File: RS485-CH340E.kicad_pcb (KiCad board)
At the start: 2 copper layers, 16.9 x 14.4 mm, 17 parts, among them J1 USB_A, J2 Conn_01x04_Male, SW1 SW_SPDT, U1 CH340E, U2 SP3485CN, U3 XC6206P332MR

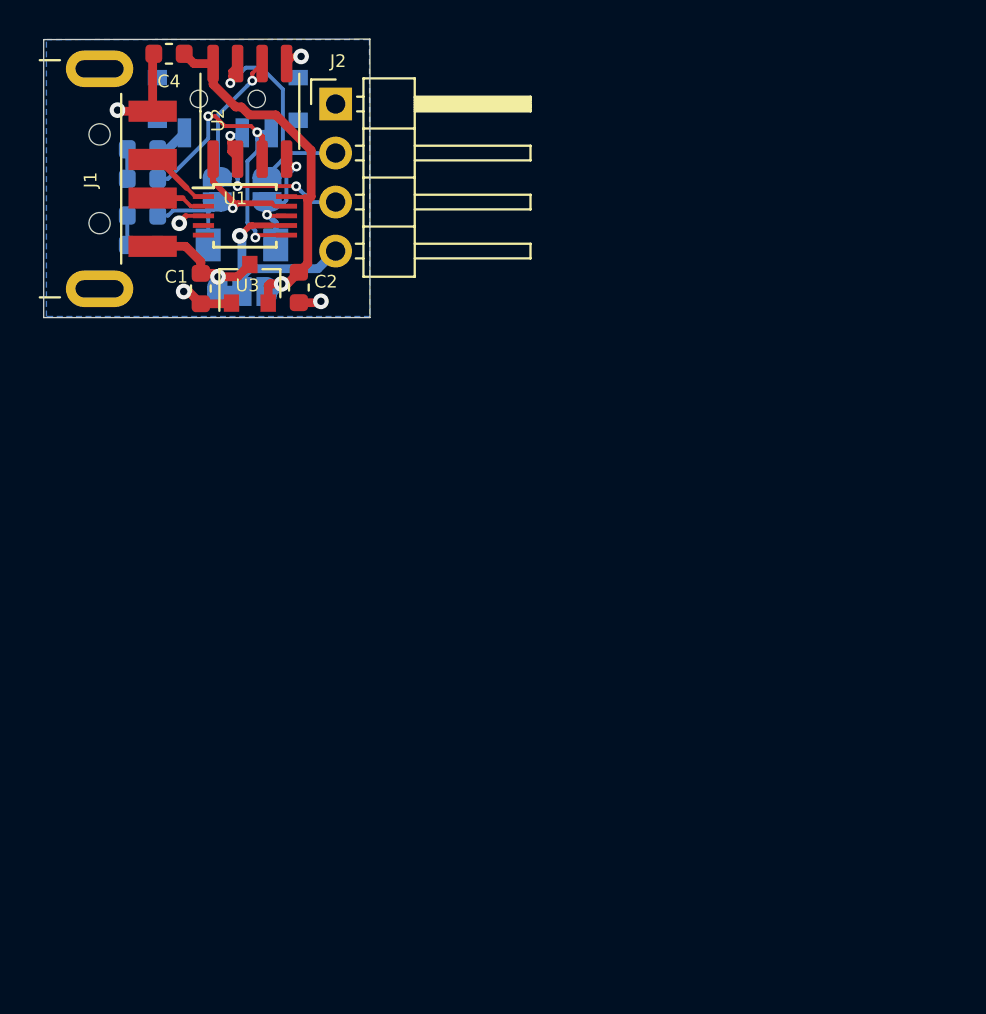
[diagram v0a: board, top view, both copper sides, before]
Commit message: Recreate kicad_sch (some files missing) Simplify & add (optional) termination & bias resistors Replace jumpers with 8-pin J3 connector Update front/back/schematic.png files
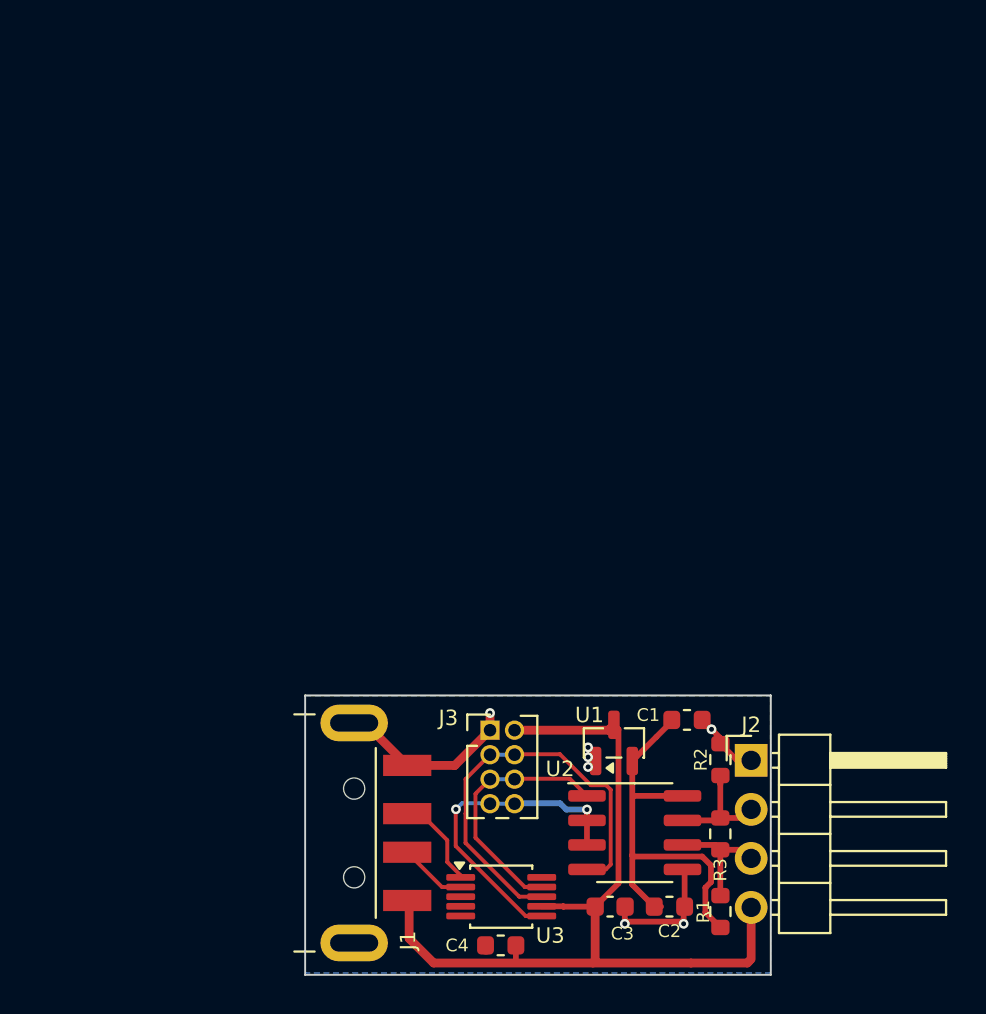
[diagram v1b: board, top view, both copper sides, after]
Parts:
- removed D1: DIODE, Diode_SMD:D_MiniMELF
- removed D2: LED red, LED_SMD:LED_0603_1608Metric
- removed D3: LED green, LED_SMD:LED_0603_1608Metric
- removed JP1: RX, Jumper:SolderJumper-2_P1.3mm_Open_RoundedPad1.0x1.5mm
- removed JP2: TX, Jumper:SolderJumper-2_P1.3mm_Open_RoundedPad1.0x1.5mm
- removed JP3: SolderJumper_3_Bridged12, Jumper:SolderJumper-3_P1.3mm_Bridged12_RoundedPad1.0x1.5mm
- removed SW1: SW_SPDT, Button_Switch_SMD:SW_SPDT_PCM12
- added C3: 1uF, Capacitor_SMD:C_0603_1608Metric, F.Cu at (144.8, 97.5)
- added J3: Conn_02x04_Odd_Even, Connector_PinHeader_1.27mm:PinHeader_2x04_P1.27mm_Vertical, F.Cu at (138.6, 88.4)
- added R3: 120, Resistor_SMD:R_0603_1608Metric, F.Cu at (150.5, 93.8)
- C1: value 1uF -> 100nF
- C4: value 100nF -> 1uF
- J2: value Conn_01x04_Male -> Conn_01x04_Pin
- R1, R2: value 4k7 -> 20K; moved to F.Cu
- U1: value CH340E -> NCP1117-3.3_SOT223; footprint Package_SO:TSSOP-10_3x3mm_P0.5mm -> Package_TO_SOT_SMD:SOT-23
- U3: value XC6206P332MR -> CH340E; footprint Package_TO_SOT_SMD:SOT-23 -> Package_SO:MSOP-10_3x3mm_P0.5mm
- moved R1 49.6 mm to (150.5, 97.8), turned to 90 degrees
- moved C4 49.3 mm to (139.1, 99.5)
- moved U2 42.4 mm to (146.1, 93.7), turned to 0 degrees
- moved J2 40.3 mm to (152.1, 90.0)
- moved R2 40.1 mm to (150.5, 89.9), turned to 90 degrees
- moved C2 37.4 mm to (147.9, 97.5), turned to 0 degrees
- moved J1 36.4 mm to (124.6, 93.7)
- moved U3 34.3 mm to (139.1, 97.0), turned to 0 degrees
- moved C1 33.7 mm to (148.8, 87.9), turned to 0 degrees
- moved U1 33.3 mm to (145.0, 89.1), turned to 90 degrees
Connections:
- C1 pad 1: VBUS -> +3.3V
- C2 pad 1: +3V3 -> +3.3V
- C4 pad 1: +3V3 -> VCC
- C4 pad 2: GND -> GND1
- J1 pad 1: VBUS -> VCC
- J1 pad 2: Net-(J1-Pad2) -> Net-(J1-D-)
- J1 pad 3: Net-(J1-Pad3) -> Net-(J1-D+)
- J2 pad 2: Net-(J2-Pad2) -> /B
- J2 pad 3: Net-(J2-Pad3) -> /A
- R1 pad 1: Net-(D2-Pad1) -> +3.3V
- R1 pad 2: GND -> /A
- R2 pad 1: Net-(D3-Pad1) -> /B
- U1 pad 1: Net-(J1-Pad3) -> GND
- U1 pad 2: Net-(J1-Pad2) -> +3.3V
- U1 pad 3: GND -> VCC
- U2 pad 2: Net-(SW1-Pad2) -> /TXE
- U2 pad 3: Net-(D2-Pad2) -> /TXE
- U2 pad 6: Net-(J2-Pad3) -> /A
- U2 pad 7: Net-(J2-Pad2) -> /B
- U2 pad 8: +3V3 -> +3.3V
- U3 pad 1: GND -> Net-(J1-D+)
- U3 pad 2: +3V3 -> Net-(J1-D-)
- U3 pad 3: VBUS -> GND
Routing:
- net VCC: track 12.9 -> 45.5 mm, vias 1 -> 0
- net +3.3V: track 0.00 -> 21.5 mm
- net +3V3: track 20.8 -> 0.00 mm, vias 1 -> 0
- net /TXE: track 0.00 -> 17.3 mm, vias 0 -> 2
- net Net-(D2-Pad2): track 17.3 -> 0.00 mm, vias 3 -> 0
- net /TxD: track 7.10 -> 22.4 mm, vias 2 -> 0
- net Net-(J2-Pad3): track 13.6 -> 0.00 mm, vias 3 -> 0
- net Net-(J2-Pad2): track 12.5 -> 0.00 mm, vias 1 -> 0
- net GND: track 12.9 -> 20.1 mm, vias 5 -> 7
- net VBUS: track 7.23 -> 0.00 mm, vias 1 -> 0
- net /B: track 0.00 -> 6.44 mm
- net /A: track 0.00 -> 6.23 mm
- net Net-(J1-D+): track 0.00 -> 4.86 mm
- net Net-(J1-D-): track 0.00 -> 3.52 mm
- net Net-(J1-Pad3): track 3.43 -> 0.00 mm
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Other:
- board size 16.9 x 14.4 mm -> 24.1 x 14.5 mm
- net class Default removed
- net class Power removed
- board text removed: "echo"

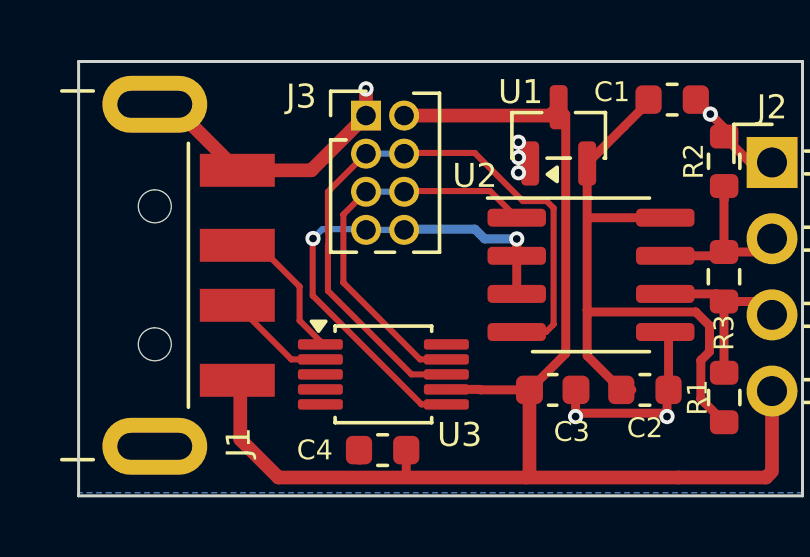
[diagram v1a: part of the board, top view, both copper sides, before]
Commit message: Update to CH340X chip (more modern) Regenerate front/back/pcb.png files
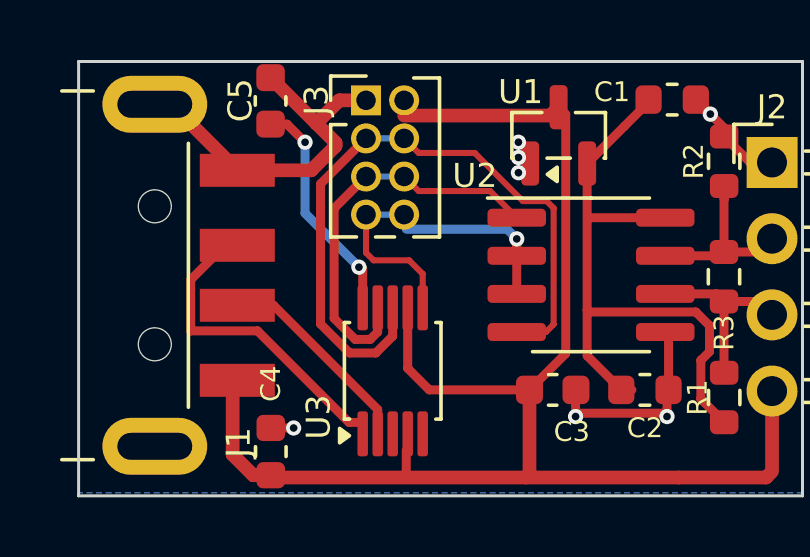
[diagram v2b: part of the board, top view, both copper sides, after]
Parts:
- added C5: 100nF, Capacitor_SMD:C_0603_1608Metric, F.Cu at (135.4, 87.9)
- U3: value CH340E -> CH340X
- moved C4 3.73 mm to (135.4, 99.6), turned to 90 degrees
- moved J3 0.51 mm to (138.6, 87.9)
- moved U3 0.33 mm to (139.4, 96.9), turned to 90 degrees
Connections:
- C4 pad 2: GND1 -> GND
- U3 pad 10: unconnected-(U3-V3-Pad10) -> Net-(U3-V3)
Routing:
- net Net-(U3-V3): track 0.00 -> 7.38 mm, vias 0 -> 2
- net Net-(J1-D+): track 4.86 -> 10.7 mm
- net /TXE: track 17.3 -> 12.1 mm, vias 2 -> 1
- net VCC: track 45.5 -> 49.6 mm
- net GND: track 20.1 -> 23.7 mm
- net Net-(J1-D-): track 3.52 -> 6.55 mm
- net /TxD: track 22.4 -> 23.2 mm
